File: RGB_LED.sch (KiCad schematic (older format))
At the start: 4 parts

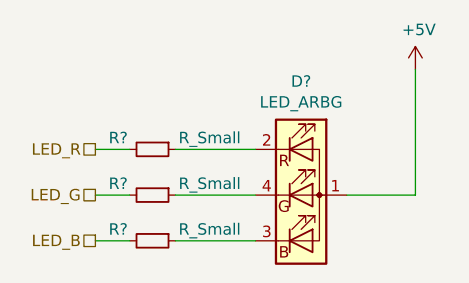
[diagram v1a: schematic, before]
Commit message: Bauteile grob platziert
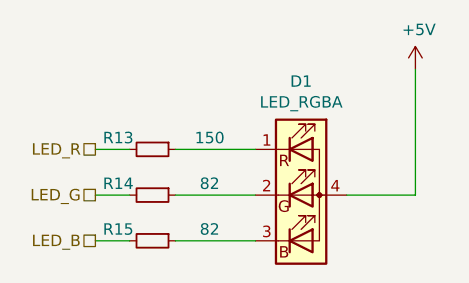
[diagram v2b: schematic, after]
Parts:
- removed D?: LED_ARBG, symbol Device:LED_ARBG
- added D1: LED_RGBA, LED_SMD:LED_Cree-PLCC4_3.2x2.8mm_CCW, symbol Device:LED_RGBA
- R13: renamed from R?; value R_Small -> 150; footprint (none) -> Resistor_SMD:R_0603_1608Metric_Pad1.05x0.95mm_HandSolder
- R14, R15: renamed from R?; value R_Small -> 82; footprint (none) -> Resistor_SMD:R_0603_1608Metric_Pad1.05x0.95mm_HandSolder
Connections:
- net +5V: now also D1.4 (A)
- net at R13.1: now also D1.1 (RK)
- net at R15.1: now also D1.3 (BK)
- net at R14.1: now also D1.2 (GK)
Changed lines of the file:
@@
 LED_B
 $Comp
-L Device:LED_ARBG D?
-U 1 1 5F040518
-P 4500 2500
-F 0 "D?" H 4500 2997 50  0000 C CNN
-F 1 "LED_ARBG" H 4500 2906 50  0000 C CNN
-F 2 "" H 4500 2450 50  0001 C CNN
-F 3 "~" H 4500 2450 50  0001 C CNN
-	1    4500 2500
-	1    0    0    -1
-$EndComp
-$Comp
-L Device:R_Small R?
+L Device:R_Small R13
 U 1 1 5F040EB8
 P 3850 2300
-F 0 "R?" V 3800 2150 50  0000 C CNN
-F 1 "R_Small" V 3800 2550 50  0000 C CNN
-F 2 "" H 3850 2300 50  0001 C CNN
+F 0 "R13" V 3800 2150 50  0000 C CNN
+F 1 "150" V 3800 2550 50  0000 C CNN
+F 2 "Resistor_SMD:R_0603_1608Metric_Pad1.05x0.95mm_HandSolder" H 3850 2300 50  0001 C CNN
 F 3 "~" H 3850 2300 50  0001 C CNN
 	1    3850 2300
@@
 $EndComp
 $Comp
-L Device:R_Small R?
+L Device:R_Small R14
 U 1 1 5F0414AB
 P 3850 2500
-F 0 "R?" V 3800 2350 50  0000 C CNN
-F 1 "R_Small" V 3800 2750 50  0000 C CNN
-F 2 "" H 3850 2500 50  0001 C CNN
+F 0 "R14" V 3800 2350 50  0000 C CNN
+F 1 "82" V 3800 2750 50  0000 C CNN
+F 2 "Resistor_SMD:R_0603_1608Metric_Pad1.05x0.95mm_HandSolder" H 3850 2500 50  0001 C CNN
 F 3 "~" H 3850 2500 50  0001 C CNN
 	1    3850 2500
@@
 $EndComp
 $Comp
-L Device:R_Small R?
+L Device:R_Small R15
 U 1 1 5F04166A
 P 3850 2700
-F 0 "R?" V 3800 2550 50  0000 C CNN
-F 1 "R_Small" V 3800 2950 50  0000 C CNN
-F 2 "" H 3850 2700 50  0001 C CNN
+F 0 "R15" V 3800 2550 50  0000 C CNN
+F 1 "82" V 3800 2950 50  0000 C CNN
+F 2 "Resistor_SMD:R_0603_1608Metric_Pad1.05x0.95mm_HandSolder" H 3850 2700 50  0001 C CNN
 F 3 "~" H 3850 2700 50  0001 C CNN
 	1    3850 2700
@@
 	3950 2700 4300 2700
 $Comp
-L power:+5V #PWR?
+L power:+5V #PWR0120
 U 1 1 5F042CCB
 P 5000 1950
-F 0 "#PWR?" H 5000 1800 50  0001 C CNN
+F 0 "#PWR0120" H 5000 1800 50  0001 C CNN
 F 1 "+5V" H 5015 2123 50  0000 C CNN
 F 2 "" H 5000 1950 50  0001 C CNN
@@
 Wire Wire Line
 	5000 2500 4700 2500
+$Comp
+L Device:LED_RGBA D1
+U 1 1 5F0771D4
+P 4500 2500
+F 0 "D1" H 4500 2997 50  0000 C CNN
+F 1 "LED_RGBA" H 4500 2906 50  0000 C CNN
+F 2 "LED_SMD:LED_Cree-PLCC4_3.2x2.8mm_CCW" H 4500 2450 50  0001 C CNN
+F 3 "~" H 4500 2450 50  0001 C CNN
+	1    4500 2500
+	1    0    0    -1
+$EndComp
 $EndSCHEMATC

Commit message: Alle Bauteile platziert
Alle Bauteile sind grob plaziert.
Einige Bauteile sollten noch umplaziert werden (u. a. die Jumper links neben Groov-Con, RGB-LED,).
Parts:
- D1: symbol Device:LED_RGBA -> MCT_Labor_5529-rescue:LED_RGBA-Device
- R13, R14, R15: symbol Device:R_Small -> MCT_Labor_5529-rescue:R_Small-Device
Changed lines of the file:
@@
 LED_B
 $Comp
-L Device:R_Small R13
+L MCT_Labor_5529-rescue:R_Small-Device R13
 U 1 1 5F040EB8
 P 3850 2300
@@
 $EndComp
 $Comp
-L Device:R_Small R14
+L MCT_Labor_5529-rescue:R_Small-Device R14
 U 1 1 5F0414AB
 P 3850 2500
@@
 $EndComp
 $Comp
-L Device:R_Small R15
+L MCT_Labor_5529-rescue:R_Small-Device R15
 U 1 1 5F04166A
 P 3850 2700
@@
 	3950 2700 4300 2700
 $Comp
-L power:+5V #PWR0120
+L MCT_Labor_5529-rescue:+5V-power #PWR0120
 U 1 1 5F042CCB
 P 5000 1950
@@
 	5000 2500 4700 2500
 $Comp
-L Device:LED_RGBA D1
+L MCT_Labor_5529-rescue:LED_RGBA-Device D1
 U 1 1 5F0771D4
 P 4500 2500

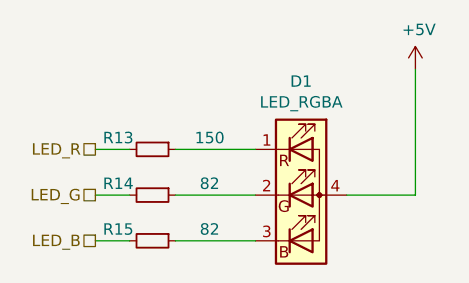
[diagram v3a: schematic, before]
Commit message: Anpassungen am Lüfteranschluss und den LEDs
-Lüfteranschluss verändert
 -> 12V-Versorgung eingefügt
-LED & LCD auf 3,3V umgestellt
 -> Ladungspunpe für neg. Kontrastspannung
-keine 5V Versorgung mehr
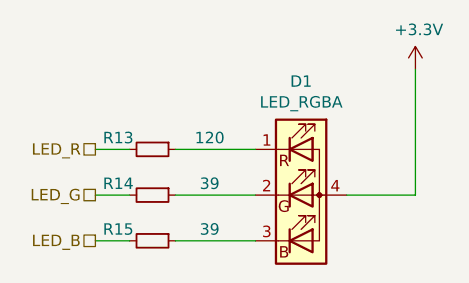
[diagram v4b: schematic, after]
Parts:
- R13: value 150 -> 120
- R14, R15: value 82 -> 39
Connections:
- net +5V renamed +3V3
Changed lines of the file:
@@
 P 3850 2300
 F 0 "R13" V 3800 2150 50  0000 C CNN
-F 1 "150" V 3800 2550 50  0000 C CNN
+F 1 "120" V 3800 2550 50  0000 C CNN
 F 2 "Resistor_SMD:R_0603_1608Metric_Pad1.05x0.95mm_HandSolder" H 3850 2300 50  0001 C CNN
 F 3 "~" H 3850 2300 50  0001 C CNN
@@
 P 3850 2500
 F 0 "R14" V 3800 2350 50  0000 C CNN
-F 1 "82" V 3800 2750 50  0000 C CNN
+F 1 "39" V 3800 2750 50  0000 C CNN
 F 2 "Resistor_SMD:R_0603_1608Metric_Pad1.05x0.95mm_HandSolder" H 3850 2500 50  0001 C CNN
 F 3 "~" H 3850 2500 50  0001 C CNN
@@
 P 3850 2700
 F 0 "R15" V 3800 2550 50  0000 C CNN
-F 1 "82" V 3800 2950 50  0000 C CNN
+F 1 "39" V 3800 2950 50  0000 C CNN
 F 2 "Resistor_SMD:R_0603_1608Metric_Pad1.05x0.95mm_HandSolder" H 3850 2700 50  0001 C CNN
 F 3 "~" H 3850 2700 50  0001 C CNN
@@
 Wire Wire Line
 	3950 2700 4300 2700
-$Comp
-L MCT_Labor_5529-rescue:+5V-power #PWR0120
-U 1 1 5F042CCB
-P 5000 1950
-F 0 "#PWR0120" H 5000 1800 50  0001 C CNN
-F 1 "+5V" H 5015 2123 50  0000 C CNN
-F 2 "" H 5000 1950 50  0001 C CNN
-F 3 "" H 5000 1950 50  0001 C CNN
-	1    5000 1950
-	1    0    0    -1
-$EndComp
 Wire Wire Line
 	5000 1950 5000 2500
@@
 	1    0    0    -1
 $EndComp
+$Comp
+L power:+3.3V #PWR017
+U 1 1 5F31ADBF
+P 5000 1950
+F 0 "#PWR017" H 5000 1800 50  0001 C CNN
+F 1 "+3.3V" H 5015 2123 50  0000 C CNN
+F 2 "" H 5000 1950 50  0001 C CNN
+F 3 "" H 5000 1950 50  0001 C CNN
+	1    5000 1950
+	1    0    0    -1
+$EndComp

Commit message: Open Hardware Logo eingefügt
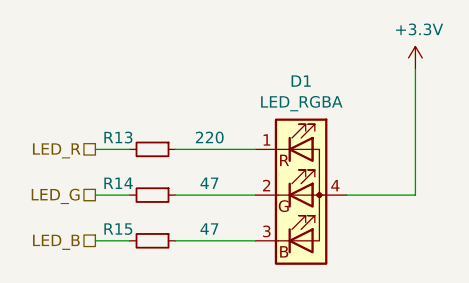
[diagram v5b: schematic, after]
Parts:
- R13: value 120 -> 220
- R14, R15: value 39 -> 47
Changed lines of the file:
@@
 P 3850 2300
 F 0 "R13" V 3800 2150 50  0000 C CNN
-F 1 "120" V 3800 2550 50  0000 C CNN
+F 1 "220" V 3800 2550 50  0000 C CNN
 F 2 "Resistor_SMD:R_0603_1608Metric_Pad1.05x0.95mm_HandSolder" H 3850 2300 50  0001 C CNN
 F 3 "~" H 3850 2300 50  0001 C CNN
@@
 P 3850 2500
 F 0 "R14" V 3800 2350 50  0000 C CNN
-F 1 "39" V 3800 2750 50  0000 C CNN
+F 1 "47" V 3800 2750 50  0000 C CNN
 F 2 "Resistor_SMD:R_0603_1608Metric_Pad1.05x0.95mm_HandSolder" H 3850 2500 50  0001 C CNN
 F 3 "~" H 3850 2500 50  0001 C CNN
@@
 P 3850 2700
 F 0 "R15" V 3800 2550 50  0000 C CNN
-F 1 "39" V 3800 2950 50  0000 C CNN
+F 1 "47" V 3800 2950 50  0000 C CNN
 F 2 "Resistor_SMD:R_0603_1608Metric_Pad1.05x0.95mm_HandSolder" H 3850 2700 50  0001 C CNN
 F 3 "~" H 3850 2700 50  0001 C CNN
